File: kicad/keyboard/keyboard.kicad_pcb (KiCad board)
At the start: 2 copper layers, 226.1 x 78.7 mm, 102 parts, among them SW1 SW_Push, SW10 SW_Push, SW11 SW_Push, SW12 SW_Push, SW13 SW_Push, SW14 SW_Push, SW15 SW_Push, SW16 SW_Push, SW17 SW_Push, SW18 SW_Push, SW19 SW_Push, SW2 SW_Push, SW20 SW_Push, SW21 SW_Push, SW22 SW_Push, SW23 SW_Push, SW24 SW_Push, SW25 SW_Push, SW26 SW_Push, SW27 SW_Push, SW28 SW_Push, SW29 SW_Push, SW3 SW_Push, SW30 SW_Push, SW31 SW_Push, SW32 SW_Push, SW33 SW_Push, SW34 SW_Push, SW35 SW_Push, SW36 SW_Push, SW37 SW_Push, SW38 SW_Push, SW39 SW_Push, SW4 SW_Push, SW40 SW_Push, SW41 SW_Push, SW42 SW_Push, SW43 SW_Push, SW44 SW_Push, SW45 SW_Push, SW46 SW_Push, SW47 SW_Push, SW48 SW_Push, SW5 SW_Push, SW6 SW_Push, SW7 SW_Push, SW8 SW_Push, SW9 SW_Push, U3 ATmega328-P, Y1 Crystal

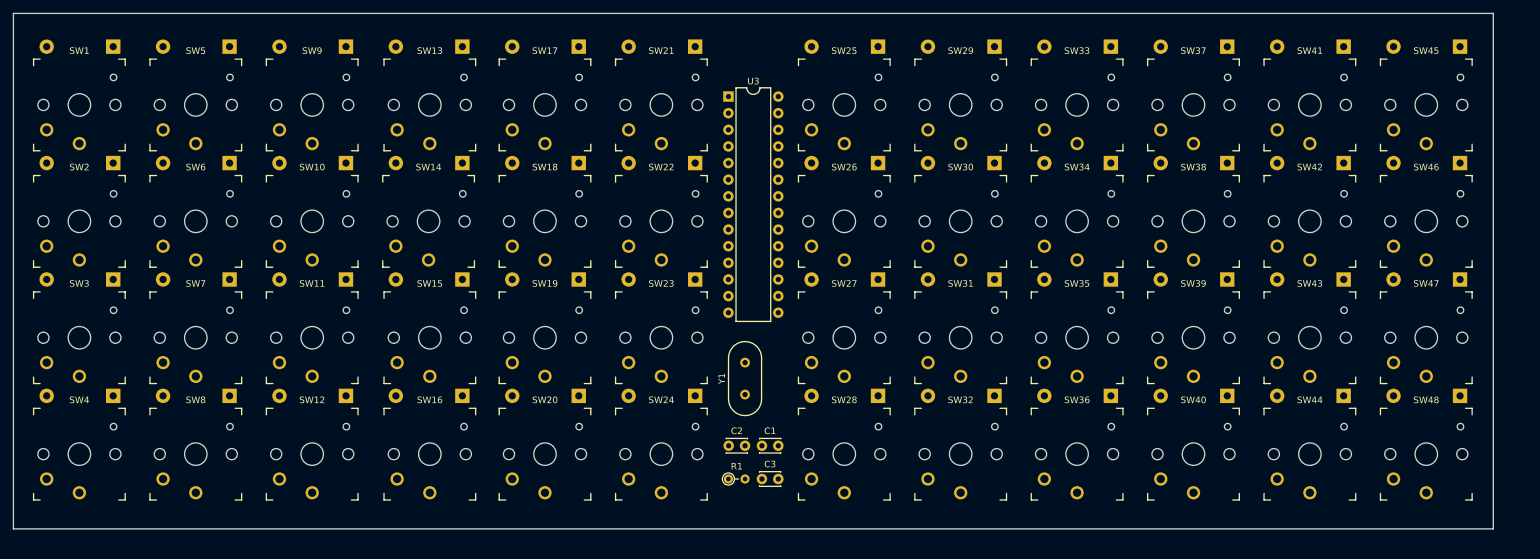
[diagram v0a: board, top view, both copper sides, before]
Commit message: Load large files from FAT16, WIP for Maze
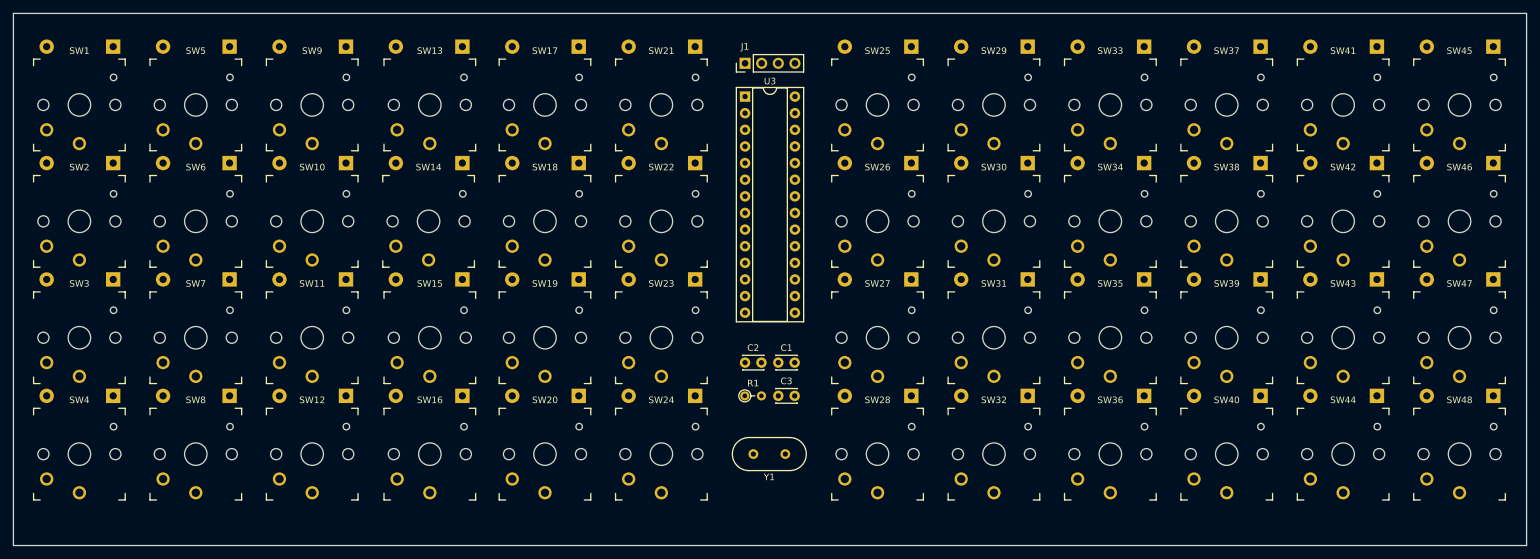
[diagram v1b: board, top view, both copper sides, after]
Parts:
- added J1: PS/2, Connector_PinHeader_2.54mm:PinHeader_1x04_P2.54mm_Vertical, F.Cu at (144.8, 40.6)
- U3: footprint Package_DIP:DIP-28_W7.62mm -> Package_DIP:DIP-28_W7.62mm_Socket
- moved C1 12.9 mm to (149.9, 86.4)
- moved C2 12.9 mm to (144.8, 86.4)
- moved C3 12.9 mm to (149.9, 91.4)
- moved R1 12.9 mm to (144.7, 91.4)
- moved Y1 11.0 mm to (150.9, 100.3), turned to 180 degrees
- moved D25 5.08 mm to (170.2, 38.1)
- moved D26 5.08 mm to (170.2, 55.9)
- moved D27 5.08 mm to (170.2, 73.7)
- moved D28 5.08 mm to (170.2, 91.4)
- moved D29 5.08 mm to (188.0, 38.1)
- moved D30 5.08 mm to (188.0, 55.9)
- moved D31 5.08 mm to (188.0, 73.7)
- moved D32 5.08 mm to (188.0, 91.4)
- moved D33 5.08 mm to (205.7, 38.1)
- moved D34 5.08 mm to (205.7, 55.9)
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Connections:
- U3 pad 11: ROW6 -> unconnected-(U3-PD5-Pad11)
- U3 pad 12: ROW7 -> PS2DATA
- U3 pad 13: ROW8 -> PS2CLK
- U3 pad 24: unconnected-(U3-PC1-Pad24) -> ROW8
- U3 pad 25: unconnected-(U3-PC2-Pad25) -> ROW7
- U3 pad 26: unconnected-(U3-PC3-Pad26) -> ROW6
- U3 pad 27: unconnected-(U3-PC4-Pad27) -> ROW5
- U3 pad 6: ROW5 -> unconnected-(U3-PD4-Pad6)
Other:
- board size 226.1 x 78.7 mm -> 231.1 x 81.3 mm

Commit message: WIP: v2.0 initial PCB
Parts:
- moved SW48 11.9 mm to (265.4, 103.3)
- moved D48 11.7 mm to (270.5, 94.0)
- moved SW47 11.6 mm to (265.4, 84.3)
- moved SW45 11.5 mm to (265.4, 46.2)
- moved SW46 11.5 mm to (265.4, 65.2)
- moved D47 11.5 mm to (270.5, 74.9)
- moved D45 11.5 mm to (270.5, 36.8)
- moved D46 11.4 mm to (270.5, 55.9)
- moved SW44 10.7 mm to (246.4, 103.3)
- moved D44 10.5 mm to (251.5, 94.0)
- moved SW43 10.4 mm to (246.4, 84.3)
- moved SW41 10.3 mm to (246.4, 46.2)
- moved SW42 10.2 mm to (246.4, 65.2)
- moved D43 10.2 mm to (251.5, 74.9)
- moved D41 10.2 mm to (251.5, 36.8)
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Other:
- board size 231.1 x 81.3 mm -> 254 x 80 mm
